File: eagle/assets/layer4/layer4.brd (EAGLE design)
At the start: 197 x 149.4 mm, 45 parts, among them Y1 8MHz

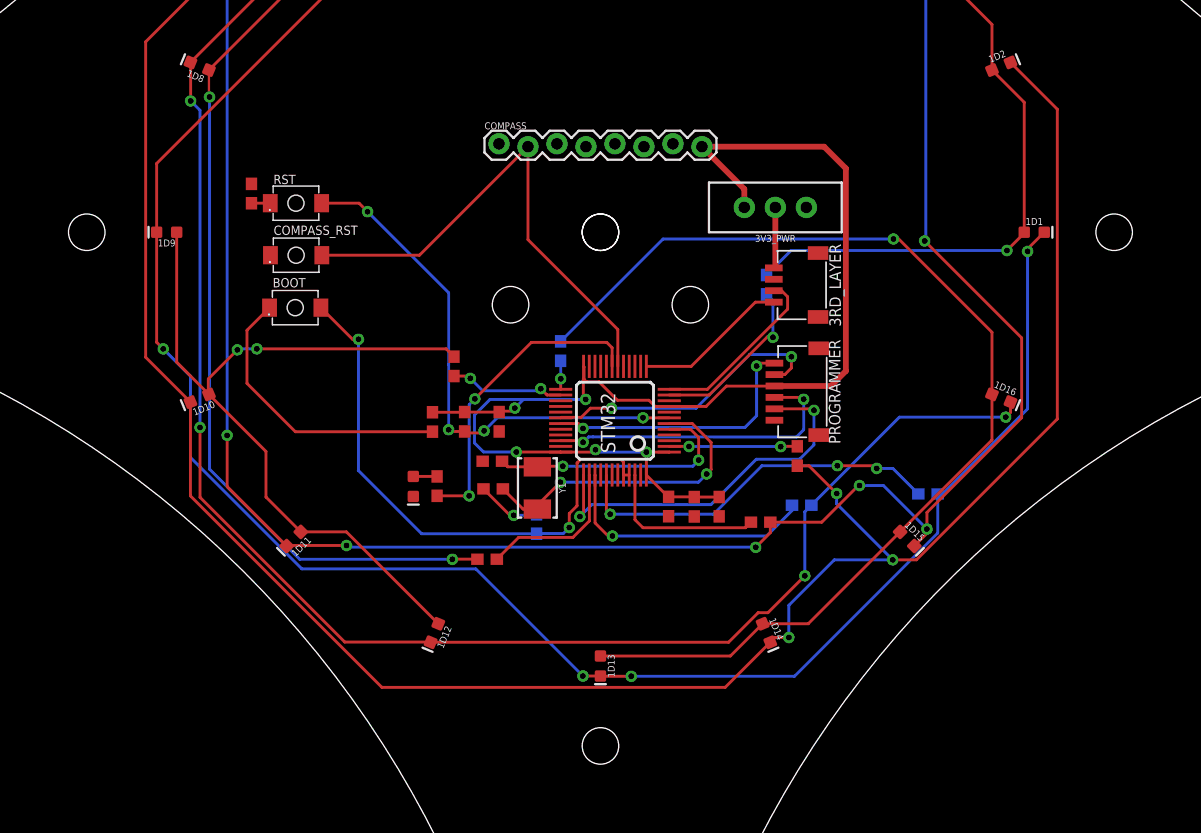
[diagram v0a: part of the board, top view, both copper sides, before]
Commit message: 🚀🚀🚀 Edited Layer 3 and 4 Changed the positioning of the BT Module Change the positioning of the connectors
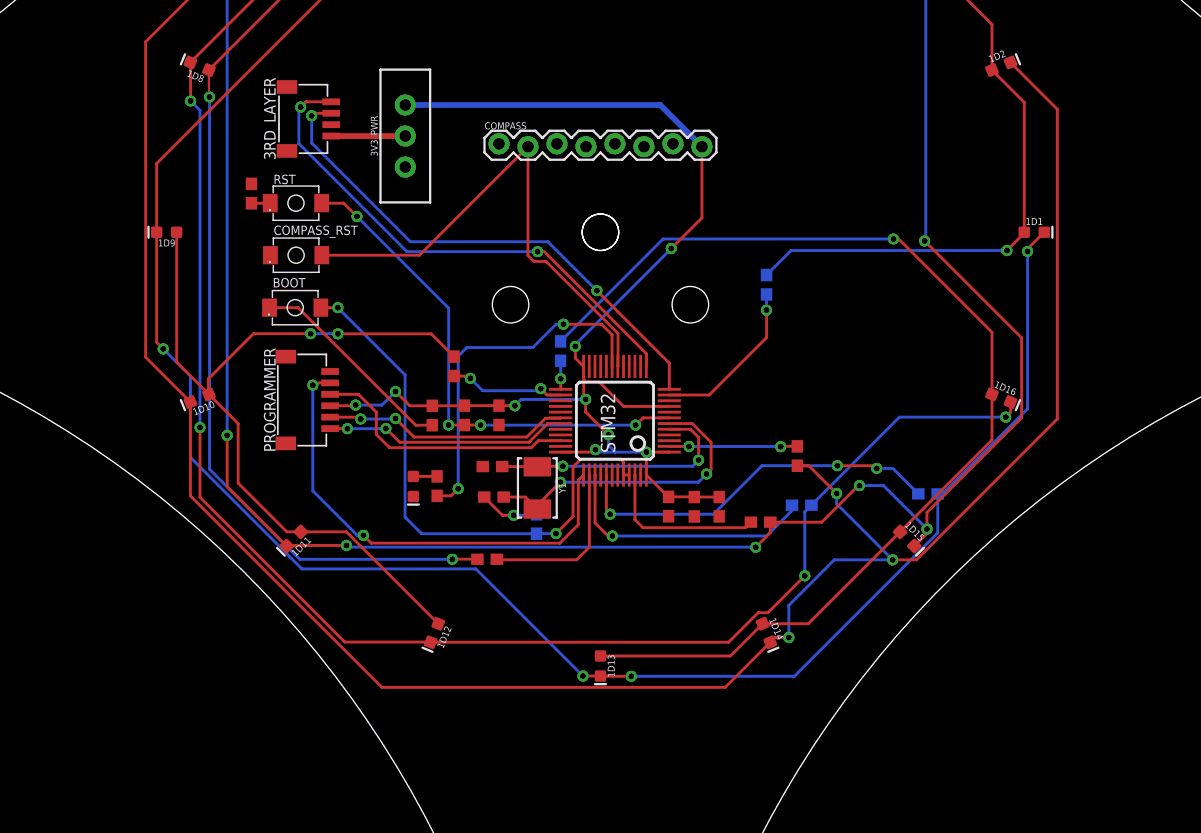
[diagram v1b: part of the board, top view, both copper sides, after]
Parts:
- moved 3RD_LAYER 41.4 mm to (-23.6, 9.92), turned to 90 degrees
- moved PROGRAMMER 38.9 mm to (-23.7, -14.7), turned to 90 degrees
- moved 3V3_PWR 33.0 mm to (-17.1, 8.43), turned to 0 degrees
- moved C7 0.72 mm to (-9.33, -23.2)
- moved R1 0.57 mm to (-11.9, -16.0)
- moved C5 0.57 mm to (-8.89, -16.0)
- moved R3 0.57 mm to (-14.7, -16.1)
- moved C6 0.47 mm to (-9.46, -20.5)
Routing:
- net RX2: track 13.5 -> 45.3 mm, vias 0 -> 2
- net TX2: track 15.8 -> 45.8 mm, vias 0 -> 2
- net SWCLK: track 33.4 -> 41.2 mm
- net N$72: track 25.5 -> 18.5 mm
- net N$73: track 27.4 -> 31.5 mm
- net TX1: track 25.3 -> 21.7 mm
- net SWDIO: track 27.1 -> 23.5 mm, vias 2 -> 0
- net 3V3_SWITCH: track 114.4 -> 111.3 mm, vias 5 -> 9
- net RX1: track 23.8 -> 21.4 mm
- net N$20: track 70.3 -> 72.1 mm
- net RESET: track 46.4 -> 44.8 mm
- net L2R: track 13.5 -> 14.9 mm
- net 3.3V: track 5.43 -> 6.49 mm
- net L1R: track 15.2 -> 14.4 mm
- net BNO_RST: track 44.5 -> 45.1 mm
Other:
- outline, holes or cut-outs redrawn

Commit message: -
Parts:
- moved 3RD_LAYER 41.4 mm to (15.2, -4.62), turned to 270 degrees
- moved PROGRAMMER 38.9 mm to (15.2, -14.0), turned to 270 degrees
- moved 3V3_PWR 33.0 mm to (15.3, 2.17), turned to 90 degrees
- moved C7 0.72 mm to (-9.40, -22.5)
- moved R1 0.57 mm to (-11.9, -16.6)
- moved C5 0.57 mm to (-8.87, -16.6)
- moved R3 0.57 mm to (-14.7, -16.6)
- moved C6 0.47 mm to (-9.47, -20.1)
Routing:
- net RX2: track 45.3 -> 13.5 mm, vias 2 -> 0
- net TX2: track 45.8 -> 15.8 mm, vias 2 -> 0
- net SWCLK: track 41.2 -> 33.4 mm
- net N$72: track 18.5 -> 25.5 mm
- net N$73: track 31.5 -> 27.4 mm
- net TX1: track 21.7 -> 25.3 mm
- net SWDIO: track 23.5 -> 27.1 mm, vias 0 -> 2
- net 3V3_SWITCH: track 111.3 -> 114.4 mm, vias 9 -> 5
- net RX1: track 21.4 -> 23.8 mm
- net N$20: track 72.1 -> 70.3 mm
- net RESET: track 44.8 -> 46.4 mm
- net L2R: track 14.9 -> 13.5 mm
- net 3.3V: track 6.49 -> 5.43 mm
- net L1R: track 14.4 -> 15.2 mm
- net BNO_RST: track 45.1 -> 44.5 mm
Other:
- outline, holes or cut-outs redrawn

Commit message: help
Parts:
- moved 3RD_LAYER 41.4 mm to (-23.6, 9.92), turned to 90 degrees
- moved PROGRAMMER 38.9 mm to (-23.7, -14.7), turned to 90 degrees
- moved 3V3_PWR 33.0 mm to (-17.1, 8.43), turned to 0 degrees
- moved C7 0.72 mm to (-9.33, -23.2)
- moved R1 0.57 mm to (-11.9, -16.0)
- moved C5 0.57 mm to (-8.89, -16.0)
- moved R3 0.57 mm to (-14.7, -16.1)
- moved C6 0.47 mm to (-9.46, -20.5)
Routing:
- net RX2: track 13.5 -> 45.3 mm, vias 0 -> 2
- net TX2: track 15.8 -> 45.8 mm, vias 0 -> 2
- net SWCLK: track 33.4 -> 41.2 mm
- net N$72: track 25.5 -> 18.5 mm
- net N$73: track 27.4 -> 31.5 mm
- net TX1: track 25.3 -> 21.7 mm
- net SWDIO: track 27.1 -> 23.5 mm, vias 2 -> 0
- net 3V3_SWITCH: track 114.4 -> 111.3 mm, vias 5 -> 9
- net RX1: track 23.8 -> 21.4 mm
- net N$20: track 70.3 -> 72.1 mm
- net RESET: track 46.4 -> 44.8 mm
- net L2R: track 13.5 -> 14.9 mm
- net 3.3V: track 5.43 -> 6.49 mm
- net L1R: track 15.2 -> 14.4 mm
- net BNO_RST: track 44.5 -> 45.1 mm
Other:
- outline, holes or cut-outs redrawn

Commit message: 🦅 Included Layer 4 new
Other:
- outline, holes or cut-outs redrawn
